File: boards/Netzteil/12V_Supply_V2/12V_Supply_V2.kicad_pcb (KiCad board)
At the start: 2 copper layers, 80 x 50 mm, 26 parts, among them P1 12V_AC, P2 12V_DC_1, P3 12V_DC_2, P4 Relais, P5 12V_DC_3, P6 12V_DC_4, P7 Relais, P8 12V_DC_5, U1 LM555N, U2 LM7812CT

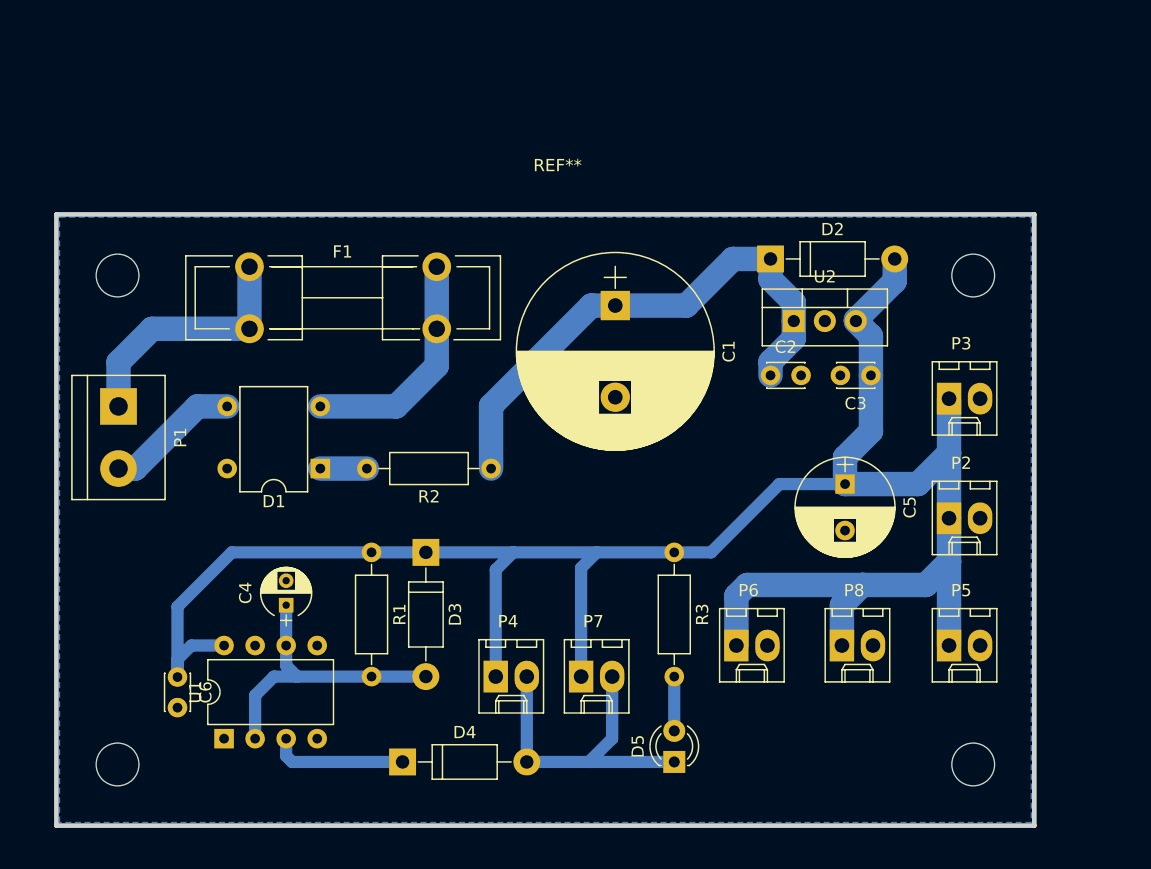
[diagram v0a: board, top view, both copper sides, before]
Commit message: Converted to Kicad 5.1 and Layout changes
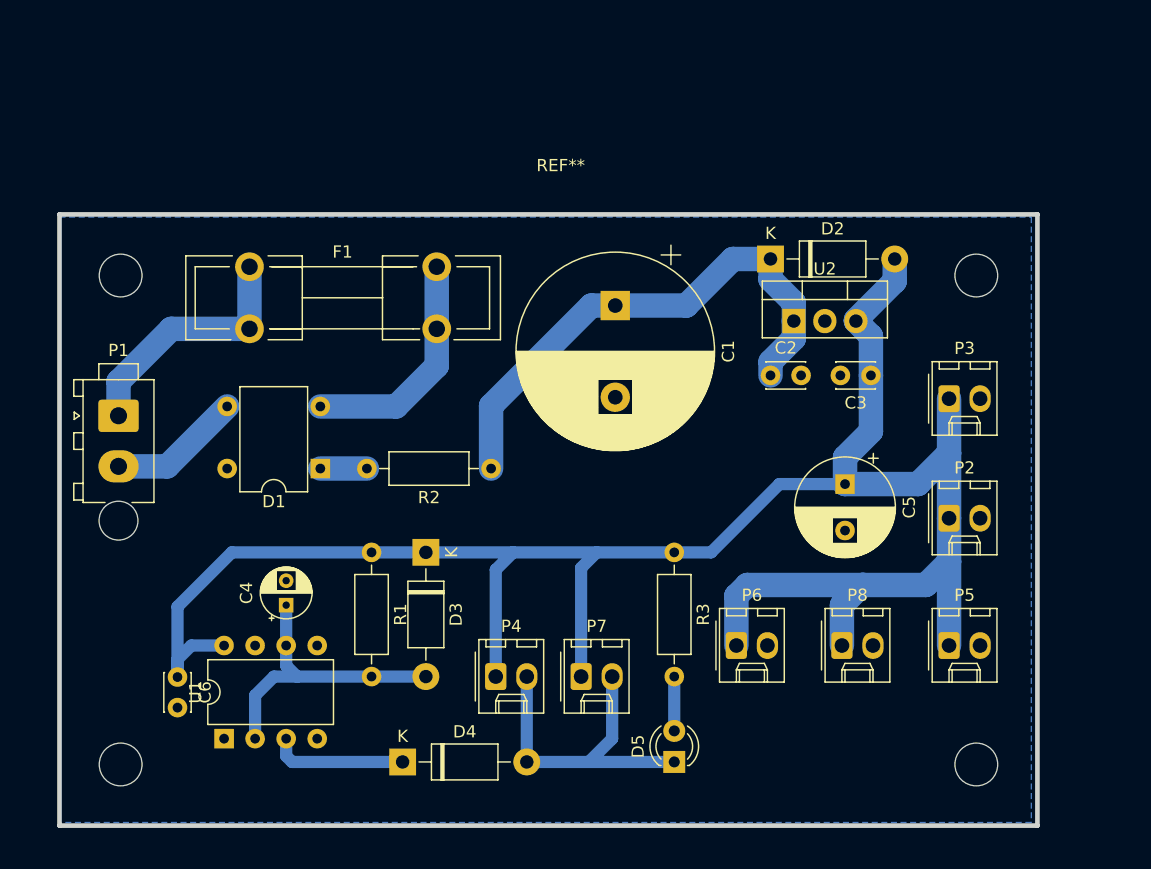
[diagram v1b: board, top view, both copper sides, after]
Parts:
- C1: footprint Capacitors_THT:CP_Radial_D16.0mm_P7.50mm -> Capacitor_THT:CP_Radial_D16.0mm_P7.50mm
- C2, C3, C6: footprint Capacitors_THT:C_Disc_D3.0mm_W2.0mm_P2.50mm -> Capacitor_THT:C_Disc_D3.0mm_W2.0mm_P2.50mm
- C4: footprint Capacitors_THT:CP_Radial_D4.0mm_P2.00mm -> Capacitor_THT:CP_Radial_D4.0mm_P2.00mm
- C5: footprint Capacitors_THT:CP_Radial_D8.0mm_P3.80mm -> Capacitor_THT:CP_Radial_D8.0mm_P3.80mm
- D1: footprint Diodes_THT:Diode_Bridge_DIP-4_W7.62mm_P5.08mm -> Diode_THT:Diode_Bridge_DIP-4_W7.62mm_P5.08mm
- D2, D3, D4: footprint Diodes_THT:D_DO-41_SOD81_P10.16mm_Horizontal -> Diode_THT:D_DO-41_SOD81_P10.16mm_Horizontal
- D5: footprint LEDs:LED_D3.0mm -> LED_THT:LED_D3.0mm
- P1: footprint Connectors_Terminal_Blocks:TerminalBlock_bornier-2_P5.08mm -> Connector_TE-Connectivity:TE_MATE-N-LOK_1-770866-x_1x02_P4.14mm_Vertical
- P2, P3, P4, P5, P6, P7, P8: footprint Connectors_Molex:Molex_KK-6410-02_02x2.54mm_Straight -> Connector_Molex:Molex_KK-254_AE-6410-02A_1x02_P2.54mm_Vertical
- R1, R2, R3: footprint Resistors_THT:R_Axial_DIN0207_L6.3mm_D2.5mm_P10.16mm_Horizontal -> Resistor_THT:R_Axial_DIN0207_L6.3mm_D2.5mm_P10.16mm_Horizontal
- U1: footprint Housings_DIP:DIP-8_W7.62mm -> Package_DIP:DIP-8_W7.62mm
- U2: footprint TO_SOT_Packages_THT:TO-220-3_Vertical -> Package_TO_SOT_THT:TO-220-3_Vertical
- moved P1 0.76 mm to (97.8, 78.2), turned to 0 degrees
- moved REF** 0.25 mm to (93.0, 111.8)
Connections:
- U1 pad 4: (no net) -> Net-(U1-Pad4)
- U1 pad 5: (no net) -> Net-(U1-Pad5)
- U1 pad 7: (no net) -> Net-(U1-Pad7)

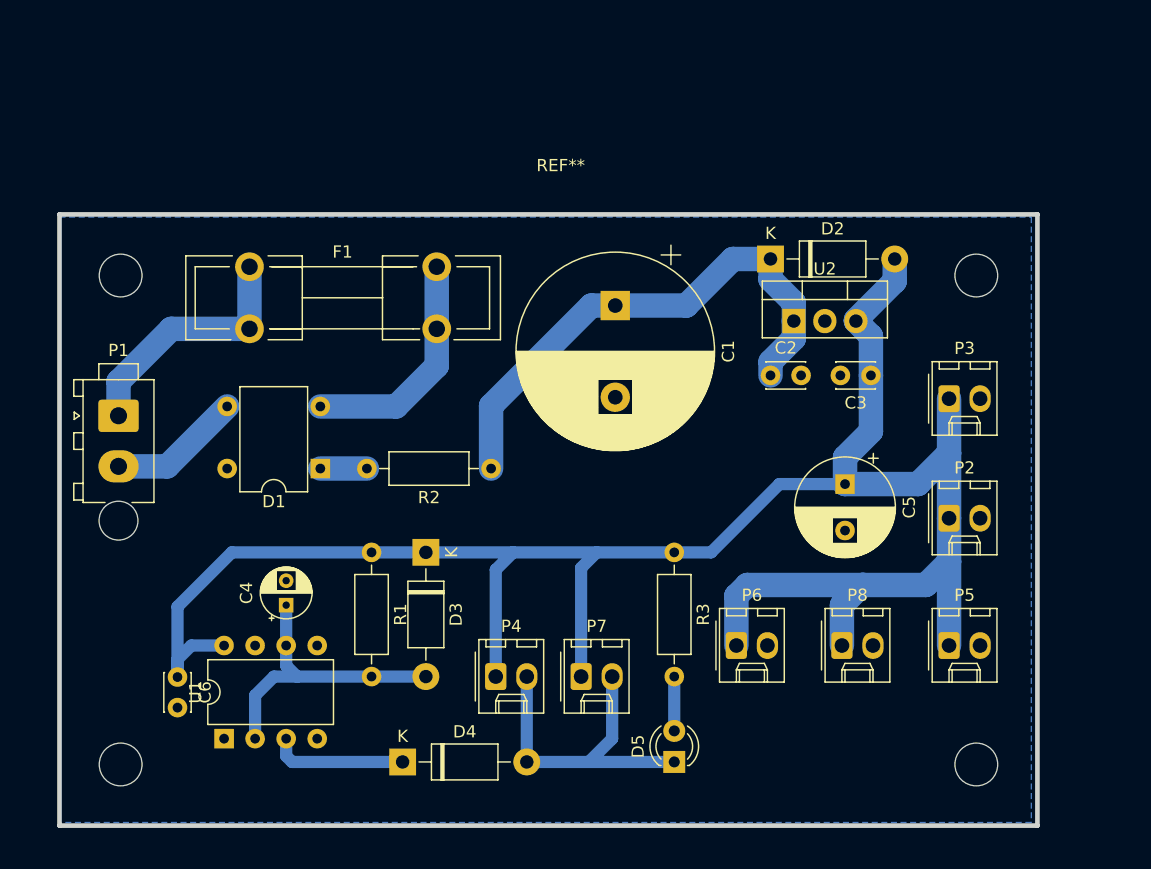
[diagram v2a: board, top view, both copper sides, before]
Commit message: HV Switch on delay added
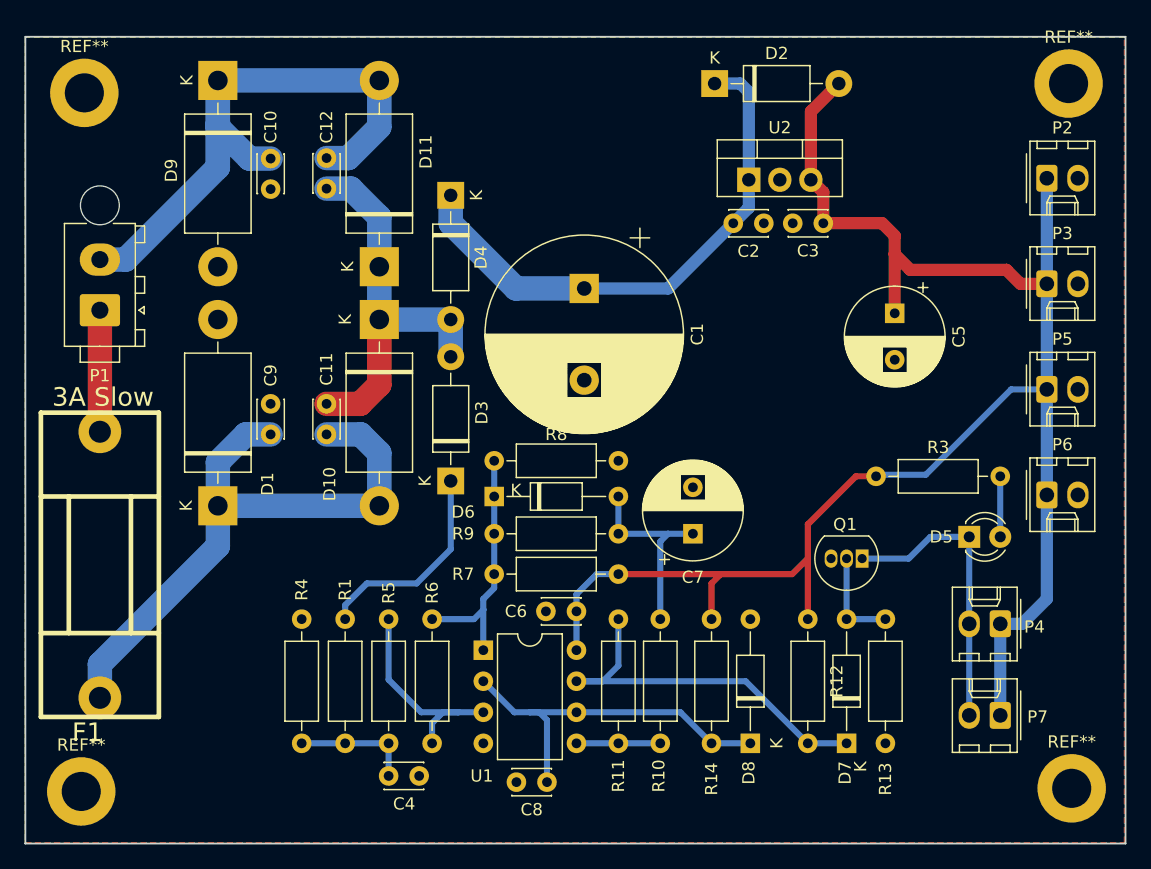
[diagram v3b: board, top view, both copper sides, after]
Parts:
- removed P8: 12V_DC_5, Connector_Molex:Molex_KK-254_AE-6410-02A_1x02_P2.54mm_Vertical
- removed R2: 10R, Resistor_THT:R_Axial_DIN0207_L6.3mm_D2.5mm_P10.16mm_Horizontal
- removed the REF** at (93.0, 111.8)
- added C10: 22nF, Capacitor_THT:C_Disc_D3.0mm_W2.0mm_P2.50mm, F.Cu at (110.2, 59.7)
- added C11: 22nF, Capacitor_THT:C_Disc_D3.0mm_W2.0mm_P2.50mm, F.Cu at (114.8, 79.8)
- added C12: 22nF, Capacitor_THT:C_Disc_D3.0mm_W2.0mm_P2.50mm, F.Cu at (114.8, 59.6)
- added C7: 47µF / 16V, Capacitor_THT:CP_Radial_D8.0mm_P3.80mm, F.Cu at (144.8, 87.9)
- added C8: 100nF / 63V, Capacitor_THT:C_Disc_D3.0mm_W2.0mm_P2.50mm, F.Cu at (132.8, 108.2)
- added C9: 22nF, Capacitor_THT:C_Disc_D3.0mm_W2.0mm_P2.50mm, F.Cu at (110.2, 79.8)
- added D10: SB350, Diode_THT:D_DO-201AD_P15.24mm_Horizontal, F.Cu at (119.1, 70.4)
- added D11: SB350, Diode_THT:D_DO-201AD_P15.24mm_Horizontal, F.Cu at (119.1, 66.0)
- added D6: 1N4148, Diode_THT:D_DO-35_SOD27_P10.16mm_Horizontal, F.Cu at (128.5, 84.8)
- added D7: ZD5V6, Diode_THT:D_DO-35_SOD27_P10.16mm_Horizontal, F.Cu at (157.4, 105.0)
- added D8: ZD3V9, Diode_THT:D_DO-35_SOD27_P10.16mm_Horizontal, F.Cu at (149.5, 105.0)
- added D9: SB350, Diode_THT:D_DO-201AD_P15.24mm_Horizontal, F.Cu at (105.9, 50.8)
- added Q1: BS170, Package_TO_SOT_THT:TO-92_Inline, F.Cu at (158.6, 89.9)
- added R10: 10K, Resistor_THT:R_Axial_DIN0207_L6.3mm_D2.5mm_P10.16mm_Horizontal, F.Cu at (142.1, 94.9)
- added R11: 5M1, Resistor_THT:R_Axial_DIN0207_L6.3mm_D2.5mm_P10.16mm_Horizontal, F.Cu at (138.7, 105.0)
- added R12: 10K, Resistor_THT:R_Axial_DIN0207_L6.3mm_D2.5mm_P10.16mm_Horizontal, F.Cu at (154.2, 94.9)
- added R13: 10K, Resistor_THT:R_Axial_DIN0207_L6.3mm_D2.5mm_P10.16mm_Horizontal, F.Cu at (160.5, 94.9)
- added R14: 4K7, Resistor_THT:R_Axial_DIN0207_L6.3mm_D2.5mm_P10.16mm_Horizontal, F.Cu at (146.3, 94.9)
- added R4: 100K, Resistor_THT:R_Axial_DIN0207_L6.3mm_D2.5mm_P10.16mm_Horizontal, F.Cu at (112.8, 105.0)
- added R5: 10K, Resistor_THT:R_Axial_DIN0207_L6.3mm_D2.5mm_P10.16mm_Horizontal, F.Cu at (119.9, 94.9)
- added R6: 1M, Resistor_THT:R_Axial_DIN0207_L6.3mm_D2.5mm_P10.16mm_Horizontal, F.Cu at (123.4, 94.9)
- added R7: 10K, Resistor_THT:R_Axial_DIN0207_L6.3mm_D2.5mm_P10.16mm_Horizontal, F.Cu at (128.5, 91.2)
- added R8: 10K, Resistor_THT:R_Axial_DIN0207_L6.3mm_D2.5mm_P10.16mm_Horizontal, F.Cu at (138.7, 81.9)
- added R9: 470K, Resistor_THT:R_Axial_DIN0207_L6.3mm_D2.5mm_P10.16mm_Horizontal, F.Cu at (128.5, 87.9)
- added REF**: MountingHole_3.2mm_M3_DIN965_Pad, MountingHole:MountingHole_3.2mm_M3_DIN965_Pad, F.Cu at (175.8, 108.7)
- added REF**: MountingHole_3.2mm_M3_DIN965_Pad, MountingHole:MountingHole_3.2mm_M3_DIN965_Pad, F.Cu at (94.7, 109.0)
- added REF**: MountingHole_3.2mm_M3_DIN965_Pad, MountingHole:MountingHole_3.2mm_M3_DIN965_Pad, F.Cu at (175.5, 51.1)
- added REF**: MountingHole_3.2mm_M3_DIN965_Pad, MountingHole:MountingHole_3.2mm_M3_DIN965_Pad, F.Cu at (95.0, 51.8)
- C4: value 200µF -> 1µF / 16V; footprint Capacitor_THT:CP_Radial_D4.0mm_P2.00mm -> Capacitor_THT:C_Disc_D3.0mm_W2.0mm_P2.50mm
- D1: value BRIDGE -> SB350; footprint Diode_THT:Diode_Bridge_DIP-4_W7.62mm_P5.08mm -> Diode_THT:D_DO-201AD_P15.24mm_Horizontal
- D3: value 1N4001 -> SB190
- D4: value 1N4001 -> SB350
- F1: value F_Small -> 3A Slow; footprint Fuse_Holders_and_Fuses:Fuseholder5x20_horiz_open_lateral_Type-II -> w_misc_comp:fuse_holder_CQ-2
- R1: value 47k -> 82K
- U1: value LM555N -> LM393
- moved D4 46.5 mm to (125.0, 60.2), turned to 270 degrees
- moved P4 41.5 mm to (169.9, 95.2), turned to 180 degrees
- moved P7 34.4 mm to (169.9, 102.7), turned to 180 degrees
- moved C6 33.1 mm to (135.3, 94.2), turned to 180 degrees
- moved D5 30.4 mm to (167.4, 88.1), turned to 0 degrees
- moved P2 28.9 mm to (173.7, 58.8)
- moved P6 28.2 mm to (173.7, 84.7)
- moved F1 27.3 mm to (96.3, 90.4)
- moved P5 22.4 mm to (173.7, 76.1)
- moved U1 22.4 mm to (127.6, 97.4), turned to 0 degrees
- moved R3 17.6 mm to (159.8, 83.2), turned to 0 degrees
- moved C4 16.3 mm to (119.9, 107.7), turned to 0 degrees
- moved D2 15.1 mm to (146.6, 51.1)
- moved C5 14.5 mm to (161.3, 69.8)
- moved C3 13.0 mm to (155.4, 62.5)
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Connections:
- D1 pad 1: Net-(D1-Pad1) -> Net-(C11-Pad1)
- D1 pad 2: Net-(D1-Pad2) -> GND
- D3 pad 1: +12V -> Net-(D3-Pad1)
- D3 pad 2: Net-(C4-Pad1) -> Net-(C11-Pad2)
- D4 pad 1: Net-(D4-Pad1) -> Net-(C1-Pad1)
- D4 pad 2: Net-(D4-Pad2) -> Net-(C11-Pad2)
- D5 pad 1: Net-(D4-Pad2) -> Net-(D5-Pad1)
- F1 pad 2: Net-(D1-Pad2) -> Net-(C11-Pad1)
- P1 pad 2: Net-(D1-Pad3) -> Net-(C10-Pad2)
- P4 pad 2: Net-(D4-Pad2) -> Net-(D5-Pad1)
- P7 pad 2: Net-(D4-Pad2) -> Net-(D5-Pad1)
- R1 pad 1: +12V -> Net-(D3-Pad1)
- U1 pad 1: GND -> Net-(D6-Pad1)
- U1 pad 2: Net-(C4-Pad1) -> /Vref
- U1 pad 3: Net-(D4-Pad1) -> Net-(R5-Pad1)
- U1 pad 4: Net-(U1-Pad4) -> GND
- U1 pad 6: Net-(C4-Pad1) -> /Vref
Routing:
- net Net-(C10-Pad2): track 0.00 -> 54.5 mm
- net Net-(C11-Pad1): track 0.00 -> 51.0 mm
- net Net-(C11-Pad2): track 0.00 -> 32.9 mm
- net Net-(D7-Pad1): track 0.00 -> 32.0 mm
- net /Vref: track 0.00 -> 30.7 mm
- net Net-(D4-Pad2): track 26.8 -> 0.00 mm
- net +12V: track 170.9 -> 146.1 mm
- net Net-(D5-Pad1): track 0.00 -> 24.1 mm
- net Net-(D6-Pad1): track 0.00 -> 20.4 mm
- net Net-(D1-Pad2): track 19.0 -> 0.00 mm
- net Net-(R5-Pad1): track 0.00 -> 18.0 mm
- net Net-(D3-Pad1): track 0.00 -> 17.3 mm
- net Net-(C7-Pad1): track 0.00 -> 16.4 mm
- net Net-(C4-Pad1): track 24.4 -> 9.78 mm
- net Net-(D4-Pad1): track 11.1 -> 0.00 mm
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- added copper zone on F.Cu, net GND
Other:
- board size 80 x 50 mm -> 90 x 66 mm
